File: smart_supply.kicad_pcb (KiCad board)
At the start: 2 copper layers, 35.6 x 32 mm, 22 parts, among them J2 Conn_01x05_Pin, J3 Conn_01x02_Pin, J4 Conn_01x06_Pin, J5 Conn_01x06_Pin, U5 ADE7953xCP, U7 MCP1825ST-3302E/EB, Y1 3.58M

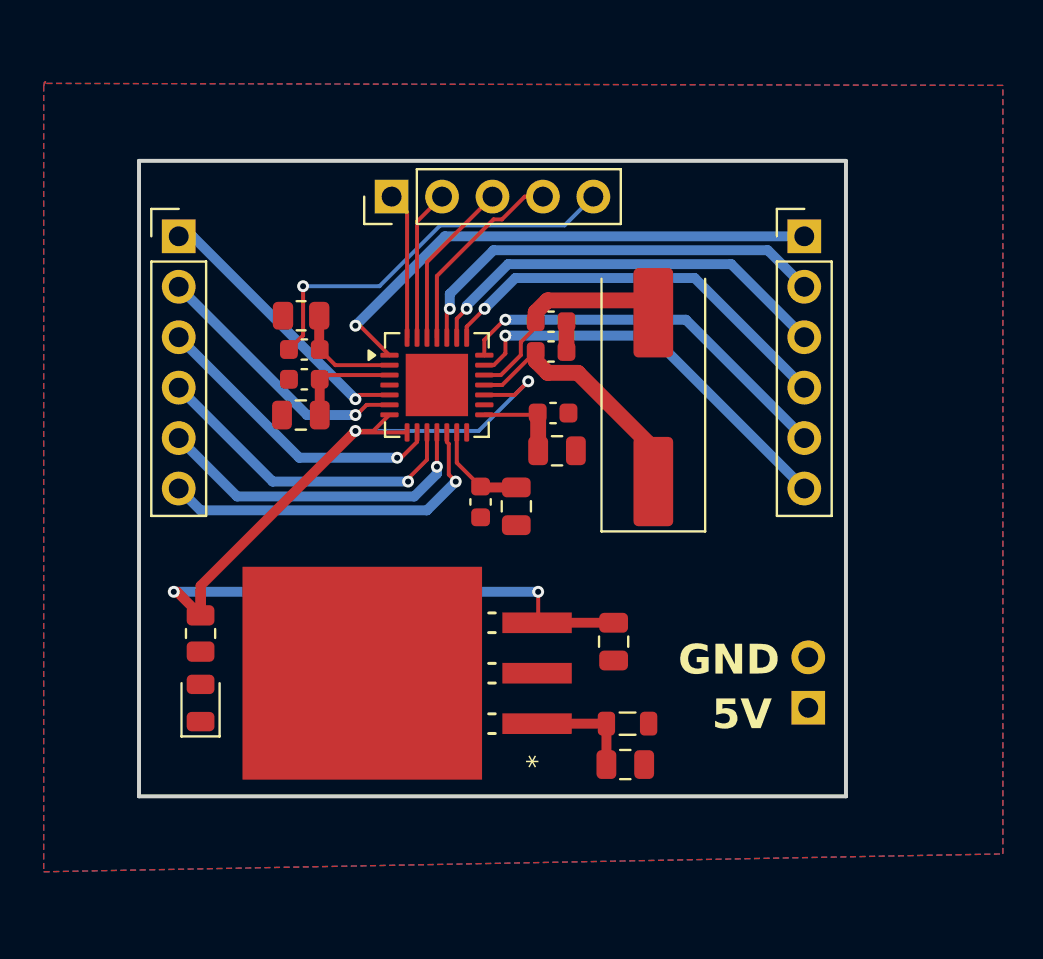
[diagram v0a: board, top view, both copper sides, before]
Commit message: add mounting holes, 3d models and small fixes
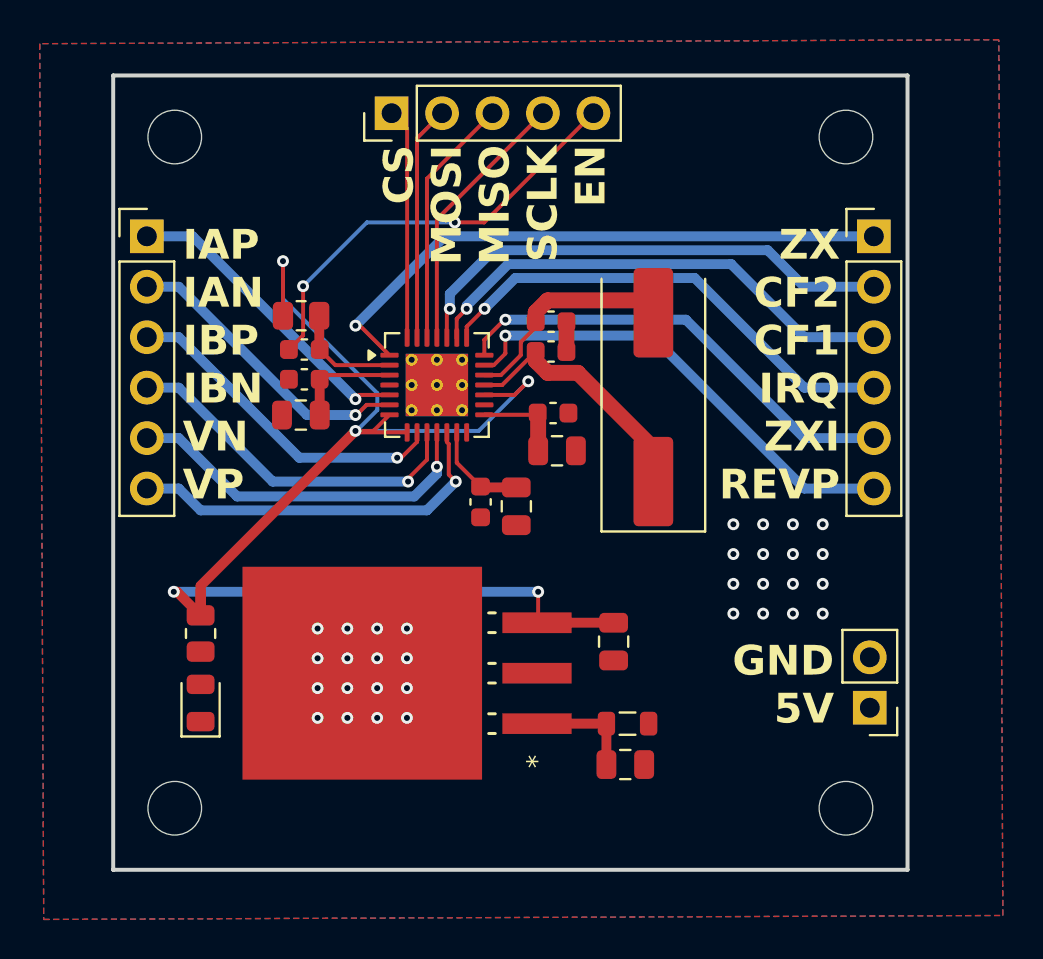
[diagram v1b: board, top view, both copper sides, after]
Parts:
- added H1: MountingHole, MountingHole:MountingHole_2.7mm_M2.5, F.Cu at (92.9, 70.6)
- added H2: MountingHole, MountingHole:MountingHole_2.7mm_M2.5, F.Cu at (126.7, 70.6)
- added H3: MountingHole, MountingHole:MountingHole_2.7mm_M2.5, F.Cu at (92.9, 36.8)
- added H4: MountingHole, MountingHole:MountingHole_2.7mm_M2.5, F.Cu at (126.7, 36.8)
- J3: moved to F.Cu
- U5: footprint Package_CSP:LFCSP-28-1EP_5x5mm_P0.5mm_EP3.14x3.14mm -> SmartSupplyLib:LFCSP-28-1EP_5x5mm_P0.5mm_EP3.14x3.14mm_ThermalVias
- moved J2 4.20 mm to (103.8, 35.6)
- moved J5 3.50 mm to (128.1, 41.8)
- moved J3 3.10 mm to (127.9, 65.5), turned to 180 degrees
- moved J4 1.60 mm to (91.5, 41.8)
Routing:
- net +3.3V: track 56.3 -> 70.1 mm, vias 4 -> 5
- net /ADE Module/MOSI: track 7.62 -> 11.8 mm
- net /ADE Module/MISO: track 8.47 -> 12.7 mm
- net /ADE Module/CS: track 7.42 -> 11.6 mm
- net /ADE Module/ZX_I: track 19.8 -> 23.3 mm
- net /ADE Module/ZX: track 26.8 -> 30.3 mm
- net /ADE Module/REVP: track 20.4 -> 24.0 mm
- net /ADE Module/IRQ: track 20.9 -> 24.4 mm
- net /ADE Module/CF2: track 21.8 -> 25.3 mm
- net /ADE Module/CF1: track 21.2 -> 24.7 mm
- net /ADE Module/SCLK: track 10.1 -> 13.5 mm
- net /ADE Module/EN: track 20.0 -> 21.7 mm, vias 1 -> 2
- net /ADE Module/VP: track 17.7 -> 19.3 mm
- net /ADE Module/VN: track 16.8 -> 18.4 mm
- net /ADE Module/IBP: track 15.3 -> 16.9 mm
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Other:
- board size 35.6 x 32 mm -> 40 x 40 mm
- board text added: "GND 5V"
- board text removed: "5V"
- board text removed: "GND"

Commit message: change ldo to a smaller one
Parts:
- U7: value MCP1825ST-3302E/EB -> MCP1825ST-3302E/DB; footprint SmartSupplyLib:DDPAK3_MC_MCH -> Package_TO_SOT_SMD:SOT-223-3_TabPin2
- moved C27 16.6 mm to (98.4, 61.8)
- moved C22 1.00 mm to (115.6, 67.4)
- moved FB2 0.81 mm to (115.6, 65.5)
- moved U7 0.70 mm to (103.0, 63.6), turned to -90 degrees
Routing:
- net +3.3V: track 70.1 -> 51.8 mm, vias 5 -> 3
- net Net-(J3-Pin_1): track 0.00 -> 11.2 mm
- net +5V: track 5.55 -> 13.3 mm
- net Net-(D5-A): track 0.00 -> 1.65 mm
- net GND: vias 32 -> 25

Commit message: created board
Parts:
- removed C15, C18: 20p, Capacitor_SMD:C_0603_1608Metric
- removed C19, C21, C24, C26: 100n, Capacitor_SMD:C_0603_1608Metric
- removed C20, C22, C23, C25: 4.7u, Capacitor_SMD:C_0805_2012Metric
- removed C27: 10u, Capacitor_SMD:C_0805_2012Metric
- removed D5: LED, LED_SMD:LED_0805_2012Metric
- removed FB2: FerriteBead_Small, Inductor_SMD:L_0805_2012Metric
- removed H1, H2, H3, H4: MountingHole, MountingHole:MountingHole_2.7mm_M2.5
- removed J2: Conn_01x05_Pin, Connector_PinHeader_2.54mm:PinHeader_1x05_P2.54mm_Vertical
- removed J3: Conn_01x02_Pin, Connector_PinHeader_2.54mm:PinHeader_1x02_P2.54mm_Vertical
- removed J4, J5: Conn_01x06_Pin, Connector_PinHeader_2.54mm:PinHeader_1x06_P2.54mm_Vertical
- removed R11: 10k, Resistor_SMD:R_0805_2012Metric
- removed R12: 50, Resistor_SMD:R_0805_2012Metric
- removed U5: ADE7953xCP, SmartSupplyLib:LFCSP-28-1EP_5x5mm_P0.5mm_EP3.14x3.14mm_ThermalVias
- removed U7: MCP1825ST-3302E/DB, Package_TO_SOT_SMD:SOT-223-3_TabPin2
- removed Y1: 3.58M, Crystal:Crystal_SMD_HC49-SD
- added C14: 10u, Capacitor_SMD:C_0805_2012Metric, F.Cu at (193.9, 106.6)
- added C2: 22u, Capacitor_SMD:C_1206_3216Metric, F.Cu at (168.6, 109.0)
- added C28: 4.7u, Capacitor_SMD:C_0805_2012Metric, F.Cu at (156.8, 123.3)
- added C29: 4.7u, Capacitor_SMD:C_0805_2012Metric, F.Cu at (156.8, 126.3)
- added C30: 100n, Capacitor_SMD:C_0805_2012Metric, F.Cu at (156.8, 129.3)
- added C31: 100n, Capacitor_SMD:C_0805_2012Metric, F.Cu at (156.8, 132.4)
- added C32: 4.7u, Capacitor_SMD:C_0805_2012Metric, F.Cu at (156.8, 135.4)
- added C33: 100n, Capacitor_SMD:C_0805_2012Metric, F.Cu at (156.8, 138.4)
- added C34: 100n, Capacitor_SMD:C_0805_2012Metric, F.Cu at (156.8, 141.4)
- added C35: 20p, Capacitor_SMD:C_0805_2012Metric, F.Cu at (161.2, 123.3)
- added C36: 20p, Capacitor_SMD:C_0805_2012Metric, F.Cu at (161.2, 126.3)
- added C37: 100n, Capacitor_SMD:C_0805_2012Metric, F.Cu at (161.2, 129.3)
- added C38: 100n, Capacitor_SMD:C_0805_2012Metric, F.Cu at (161.2, 132.4)
- added C39: 33n, Capacitor_SMD:C_0805_2012Metric, F.Cu at (130.2, 101.3)
- added C40: 33n, Capacitor_SMD:C_0805_2012Metric, F.Cu at (130.2, 104.3)
- added C41: 33n, Capacitor_SMD:C_0805_2012Metric, F.Cu at (130.2, 107.3)
- added C42: 33n, Capacitor_SMD:C_0805_2012Metric, F.Cu at (130.2, 110.3)
- added C43: 33n, Capacitor_SMD:C_0805_2012Metric, F.Cu at (130.2, 113.3)
- added C44: 33n, Capacitor_SMD:C_0805_2012Metric, F.Cu at (130.2, 116.3)
- added C45: 33n, Capacitor_SMD:C_0805_2012Metric, F.Cu at (130.2, 119.3)
- added C46: 33n, Capacitor_SMD:C_0805_2012Metric, F.Cu at (130.2, 122.3)
- added C47: 20p, Capacitor_SMD:C_0805_2012Metric, F.Cu at (161.2, 135.4)
- added C48: 20p, Capacitor_SMD:C_0805_2012Metric, F.Cu at (161.2, 138.4)
- added C49: 4.7u, Capacitor_SMD:C_0805_2012Metric, F.Cu at (161.2, 141.4)
- added C5: 220u, Capacitor_THT:C_Axial_L12.0mm_D6.5mm_P15.00mm_Horizontal, F.Cu at (156.1, 100.0)
- added C50: 4.7u, Capacitor_SMD:C_0805_2012Metric, F.Cu at (165.7, 123.3)
- added C51: 100n, Capacitor_SMD:C_0805_2012Metric, F.Cu at (165.7, 126.3)
- added C52: 100n, Capacitor_SMD:C_0805_2012Metric, F.Cu at (193.9, 109.6)
- added C53: 4.7u, Capacitor_SMD:C_0805_2012Metric, F.Cu at (165.7, 129.3)
- added C54: 100n, Capacitor_SMD:C_0805_2012Metric, F.Cu at (193.9, 112.6)
- added C55: 4.7u, Capacitor_SMD:C_0805_2012Metric, F.Cu at (198.4, 106.6)
- added C56: 10u, Capacitor_SMD:C_1206_3216Metric, F.Cu at (168.6, 112.3)
- added C57: 100n, Capacitor_SMD:C_0805_2012Metric, F.Cu at (198.4, 109.6)
- added C58: 100n, Capacitor_SMD:C_0805_2012Metric, F.Cu at (198.4, 112.6)
- added C59: 100n, Capacitor_SMD:C_0805_2012Metric, F.Cu at (202.8, 106.6)
- added C60: 100n, Capacitor_SMD:C_0805_2012Metric, F.Cu at (202.8, 109.6)
- added C61: 10u, Capacitor_SMD:C_1206_3216Metric, F.Cu at (157.3, 144.6)
- added C62: 100n, Capacitor_SMD:C_0805_2012Metric, F.Cu at (165.7, 132.4)
- added C63: 10u, Capacitor_SMD:C_1206_3216Metric, F.Cu at (157.3, 147.9)
- added C64: 100n, Capacitor_SMD:C_0805_2012Metric, F.Cu at (165.7, 135.4)
- added Csns1: ZMCT103C, Transformer_THT:Transformer_Zeming_ZMCT103C, F.Cu at (136.7, 105.9)
- added Csns2: ZMCT103C, Transformer_THT:Transformer_Zeming_ZMCT103C, F.Cu at (136.7, 117.8)
- added D10: 1N4007, Diode_THT:D_DO-41_SOD81_P10.16mm_Horizontal, F.Cu at (88.4, 127.2)
- added D11: LED, LED_THT:LED_D5.0mm, F.Cu at (186.9, 125.6)
- added D12: LED, LED_THT:LED_D5.0mm, F.Cu at (186.9, 133.0)
- added D13: LED, LED_THT:LED_D5.0mm, F.Cu at (186.9, 140.5)
- added D14: TPD1E10B06DPYR, SmartSupplyLib:TPD1E10B06DPYR, F.Cu at (212.8, 102.8)
- added D15: SMF5V0A, Diode_SMD:D_SMF, F.Cu at (168.7, 105.7)
- added D16: LED, LED_SMD:LED_0805_2012Metric, F.Cu at (216.2, 59.0)
- added D17: LED, LED_SMD:LED_0805_2012Metric, F.Cu at (216.2, 62.0)
- added D18: LED, LED_SMD:LED_0805_2012Metric, F.Cu at (216.2, 65.0)
- added D19: LED, LED_SMD:LED_0805_2012Metric, F.Cu at (162.4, 149.4)
- added D6: SS34, Diode_SMD:D_SMA, F.Cu at (213.1, 98.7)
- added D7: 1N4007, Diode_THT:D_DO-41_SOD81_P10.16mm_Horizontal, F.Cu at (88.4, 114.4)
- added D8: 1N4007, Diode_THT:D_DO-41_SOD81_P10.16mm_Horizontal, F.Cu at (88.4, 118.7)
- added D9: 1N4007, Diode_THT:D_DO-41_SOD81_P10.16mm_Horizontal, F.Cu at (88.4, 122.9)
- added F2: Fuse, SmartSupplyLib:fuse holder, F.Cu at (80.0, 24.5)
- added FB1: FerriteBead, Capacitor_SMD:C_0805_2012Metric, F.Cu at (202.8, 112.6)
- added FB4: FerriteBead, Capacitor_SMD:C_0603_1608Metric, F.Cu at (162.2, 144.2)
- added FB5: FerriteBead, Capacitor_SMD:C_0603_1608Metric, F.Cu at (162.2, 146.7)
- added H5: MountingHole, MountingHole:MountingHole_3.2mm_M3, F.Cu at (210.0, 47.5)
- added H6: MountingHole, MountingHole:MountingHole_3.2mm_M3, F.Cu at (210.0, 55.4)
- added H7: MountingHole, MountingHole:MountingHole_3.2mm_M3, F.Cu at (210.0, 63.4)
- added H8: MountingHole, MountingHole:MountingHole_3.2mm_M3, F.Cu at (210.0, 71.3)
- added IC4: MIC39100-3.3WS, SmartSupplyLib:SOT230P700X180-4N, F.Cu at (213.9, 92.2)
- added J1: USB_C_Receptacle_USB2.0_16P, Connector_USB:USB_C_Receptacle_Amphenol_124019772112A, F.Cu at (180.0, 113.9)
- added J10: DM3AT-SF-PEJM5, SmartSupplyLib:DM3ATSFPEJM5, F.Cu at (182.8, 98.3)
- added J11: 1717020, SmartSupplyLib:CONN_1717020_PXC, F.Cu at (55.5, 24.5)
- added J12: 1717020, SmartSupplyLib:CONN_1717020_PXC, F.Cu at (68.0, 24.5)
- added J13: Conn_01x06_Pin, Connector_JST:JST_XH_B6B-XH-A_1x06_P2.50mm_Vertical, F.Cu at (195.4, 125.2)
- added J14: 1730405, SmartSupplyLib:CONN_1730405_PXC, F.Cu at (74.9, 151.0)
- added J15: 1717020, SmartSupplyLib:CONN_1717020_PXC, F.Cu at (74.5, 137.0)
- added J16: Conn_01x06_Pin, Connector_JST:JST_XH_B6B-XH-A_1x06_P2.50mm_Vertical, F.Cu at (158.0, 91.5)
- added J6: 1730405, SmartSupplyLib:CONN_1730405_PXC, F.Cu at (43.5, 23.0)
- added J8: 1717020, SmartSupplyLib:CONN_1717020_PXC, F.Cu at (82.8, 52.0)
- added J9: 1717020, SmartSupplyLib:CONN_1717020_PXC, F.Cu at (95.8, 52.0)
- added K3: G2R-1A-E DC5, SmartSupplyLib:RELAY_G2R-1A-E AC12_OMR, F.Cu at (142.8, 19.3)
- added K4: G2R-1A-E DC5, SmartSupplyLib:RELAY_G2R-1A-E AC12_OMR, F.Cu at (124.5, 19.3)
- added K5: G2R-1A-E DC5, SmartSupplyLib:RELAY_G2R-1A-E AC12_OMR, F.Cu at (132.0, 75.9)
- added K6: G2R-1A-E DC5, SmartSupplyLib:RELAY_G2R-1A-E AC12_OMR, F.Cu at (150.5, 75.4)
- added Q3: AO3400A, Package_TO_SOT_SMD:SOT-23, F.Cu at (70.0, 121.0)
- added Q4: AO3400A, Package_TO_SOT_SMD:SOT-23, F.Cu at (70.0, 125.4)
- added R17: 10k, Resistor_SMD:R_0805_2012Metric, F.Cu at (170.1, 123.3)
- added R19: 10k, Resistor_SMD:R_0805_2012Metric, F.Cu at (207.3, 118.3)
- added R2: 0, Resistor_SMD:R_0805_2012Metric, F.Cu at (207.3, 106.5)
- added R20: 10k, Resistor_SMD:R_0805_2012Metric, F.Cu at (211.7, 106.5)
- added R21: 10k, Resistor_SMD:R_0805_2012Metric, F.Cu at (211.7, 109.5)
- added R22: 10k, Resistor_SMD:R_0805_2012Metric, F.Cu at (211.7, 112.5)
- added R23: 10k, Resistor_SMD:R_0805_2012Metric, F.Cu at (211.7, 115.4)
- added R24: 10k, Resistor_SMD:R_0805_2012Metric, F.Cu at (170.1, 126.2)
- added R25: 10k, Resistor_SMD:R_0805_2012Metric, F.Cu at (170.1, 129.2)
- added R26: 47k, Resistor_THT:R_Axial_DIN0414_L11.9mm_D4.5mm_P20.32mm_Horizontal, F.Cu at (130.0, 90.7)
- added R27: 47k, Resistor_THT:R_Axial_DIN0414_L11.9mm_D4.5mm_P20.32mm_Horizontal, F.Cu at (130.0, 96.7)
- added R28: 100, Resistor_SMD:R_0805_2012Metric, F.Cu at (69.7, 102.5)
- added R29: 1k, Resistor_SMD:R_0805_2012Metric, F.Cu at (69.7, 105.5)
- added R30: 1k, Resistor_SMD:R_0805_2012Metric, F.Cu at (69.7, 108.4)
- added R31: 1k, Resistor_SMD:R_0805_2012Metric, F.Cu at (69.7, 111.4)
- added R32: 10, Resistor_SMD:R_0603_1608Metric, F.Cu at (102.5, 113.6)
- added R33: 10, Resistor_SMD:R_0603_1608Metric, F.Cu at (102.5, 116.1)
- added R34: 1k, Resistor_SMD:R_0805_2012Metric, F.Cu at (69.7, 114.3)
- added R35: 1.5k, Resistor_SMD:R_0805_2012Metric, F.Cu at (211.7, 118.3)
- added R36: 20k, Resistor_SMD:R_0805_2012Metric, F.Cu at (69.7, 117.3)
- added R37: 1k, Resistor_SMD:R_0805_2012Metric, F.Cu at (74.1, 102.5)
- added R38: 100, Resistor_SMD:R_0805_2012Metric, F.Cu at (74.1, 105.5)
- added R39: 1k, Resistor_SMD:R_0805_2012Metric, F.Cu at (74.1, 108.4)
- added R40: 33, Resistor_SMD:R_0603_1608Metric, F.Cu at (102.5, 118.6)
- added R41: 33, Resistor_SMD:R_0603_1608Metric, F.Cu at (102.5, 121.1)
- added R42: 1k, Resistor_SMD:R_0805_2012Metric, F.Cu at (74.1, 111.4)
- added R43: 1k, Resistor_SMD:R_0805_2012Metric, F.Cu at (74.1, 114.3)
- added R44: 10k, Resistor_SMD:R_0805_2012Metric, F.Cu at (170.1, 132.2)
- added R45: 10k, Resistor_SMD:R_0805_2012Metric, F.Cu at (170.1, 135.1)
- added R46: 270, Resistor_SMD:R_0805_2012Metric, F.Cu at (194.2, 131.1)
- added R47: 270, Resistor_SMD:R_0805_2012Metric, F.Cu at (194.2, 134.1)
- added R48: 270, Resistor_SMD:R_0805_2012Metric, F.Cu at (194.2, 137.0)
- added R49: 10k, Resistor_SMD:R_0805_2012Metric, F.Cu at (216.1, 106.5)
- added R5: 10k, Resistor_SMD:R_0805_2012Metric, F.Cu at (207.3, 109.5)
- added R50: 100, Resistor_SMD:R_0805_2012Metric, F.Cu at (74.1, 117.3)
- added R51: 100k, Resistor_SMD:R_0805_2012Metric, F.Cu at (78.5, 102.5)
- added R52: 100, Resistor_SMD:R_0805_2012Metric, F.Cu at (78.5, 105.5)
- added R53: 100k, Resistor_SMD:R_0805_2012Metric, F.Cu at (78.5, 108.4)
- added R54: 470, Resistor_SMD:R_0805_2012Metric, F.Cu at (216.1, 109.5)
- added R55: 470, Resistor_SMD:R_0805_2012Metric, F.Cu at (216.1, 112.5)
- added R56: 470, Resistor_SMD:R_0805_2012Metric, F.Cu at (216.1, 115.4)
- added R57: 470, Resistor_SMD:R_0805_2012Metric, F.Cu at (170.1, 138.1)
- added R6: 5.1k, Resistor_SMD:R_0805_2012Metric, F.Cu at (207.3, 112.5)
- added R7: 5.1k, Resistor_SMD:R_0805_2012Metric, F.Cu at (207.3, 115.4)
- added RV1: MOV-14D241K, SmartSupplyLib:MOV14D241K, F.Cu at (113.0, 30.5)
- added SW1: SW_Push, Button_Switch_SMD:SW_SPST_Omron_B3FS-100xP, F.Cu at (160.2, 107.9)
- added SW2: SW_Push, Button_Switch_SMD:SW_SPST_Omron_B3FS-100xP, F.Cu at (160.2, 115.8)
- added TP1: TestPoint, TestPoint:TestPoint_Loop_D2.50mm_Drill1.0mm, F.Cu at (216.3, 45.8)
- added TP2: TestPoint, TestPoint:TestPoint_Loop_D2.50mm_Drill1.0mm, F.Cu at (216.3, 50.5)
- added TP3: TestPoint, TestPoint:TestPoint_Loop_D2.50mm_Drill1.0mm, F.Cu at (216.3, 55.1)
- added U1: ESP32-S3-MINI-1U, RF_Module:ESP32-S2-MINI-1U, F.Cu at (200.6, 96.6)
- added U10: ADE7953xCP, Package_CSP:LFCSP-28-1EP_5x5mm_P0.5mm_EP3.14x3.14mm, F.Cu at (176.3, 132.7)
- added U4: HLK-10M05, Converter_ACDC:Converter_ACDC_Hi-Link_HLK-10Mxx, F.Cu at (58.0, 48.0)
- added U6: USBLC6-2SC6, Package_TO_SOT_SMD:SOT-23-6, F.Cu at (168.3, 116.4)
- added U8: ADE7953xCP, Package_CSP:LFCSP-28-1EP_5x5mm_P0.5mm_EP3.14x3.14mm, F.Cu at (176.3, 125.5)
- added Vsns1: ZMPT101K, Transformer_THT:Transformer_Zeming_ZMPT101K, F.Cu at (92.1, 77.2)
- added Vsns2: ZMPT101K, Transformer_THT:Transformer_Zeming_ZMPT101K, F.Cu at (92.1, 96.4)
- added Y2: 3.58M, Crystal:Crystal_SMD_HC49-SD, F.Cu at (175.2, 142.9)
- added Y3: 3.58M, Crystal:Crystal_SMD_HC49-SD, F.Cu at (175.2, 149.7)
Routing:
- net +3.3V: track 51.8 -> 0.00 mm, vias 3 -> 0
- net /ADE Module/ZX: track 30.3 -> 0.00 mm, vias 1 -> 0
- net /ADE Module/CF2: track 25.3 -> 0.00 mm, vias 1 -> 0
- net /ADE Module/CF1: track 24.7 -> 0.00 mm, vias 1 -> 0
- net /ADE Module/IRQ: track 24.4 -> 0.00 mm, vias 1 -> 0
- net /ADE Module/REVP: track 24.0 -> 0.00 mm, vias 1 -> 0
- net /ADE Module/ZX_I: track 23.3 -> 0.00 mm, vias 1 -> 0
- net /ADE Module/EN: track 21.7 -> 0.00 mm, vias 2 -> 0
- net /ADE Module/VP: track 19.3 -> 0.00 mm, vias 1 -> 0
- net /ADE Module/VN: track 18.4 -> 0.00 mm, vias 1 -> 0
- net /ADE Module/IBN: track 18.0 -> 0.00 mm, vias 1 -> 0
- net /ADE Module/IBP: track 16.9 -> 0.00 mm, vias 1 -> 0
- net /ADE Module/IAP: track 15.7 -> 0.00 mm, vias 1 -> 0
- net /ADE Module/IAN: track 15.1 -> 0.00 mm, vias 1 -> 0
- net /ADE Module/CLKIN: track 13.6 -> 0.00 mm
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- removed copper zone on B.Cu, net GND
- removed copper zone on F.Cu, net GND
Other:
- board size 40 x 40 mm -> 200 x 150 mm
- board text removed: "ADE7953 Breakout Board"
- board text removed: "CS MOSI MISO SCLK EN"
- board text removed: "GND 5V"
- board text removed: "IAP IAN IBP IBN VN VP"
- board text removed: "ZX CF2 CF1 IRQ ZXI REVP"
